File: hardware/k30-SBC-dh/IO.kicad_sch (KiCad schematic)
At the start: 26 parts, among them J1 CompactFlash, J2 Serial1, J3 Serial2, SW3 IP2, SW4 IP3, U13 MC68681, U7 74HC32, Y2 Crystal

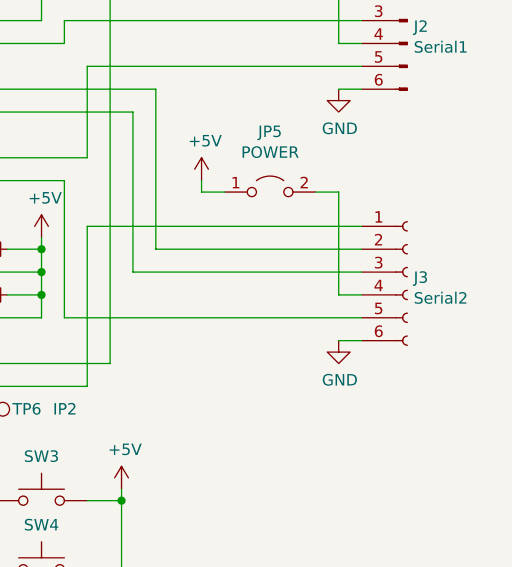
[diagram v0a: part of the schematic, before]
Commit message: use 5.08mm 1x2 screw terminal for power
These are good for 6A.

Noted on the silkscreen that this is a modified version
of the PCB.
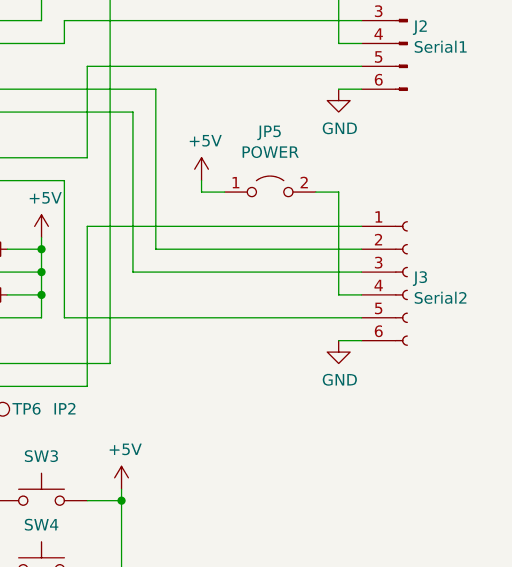
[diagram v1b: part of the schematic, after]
